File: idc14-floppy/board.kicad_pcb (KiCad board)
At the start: 2 copper layers, 81.3 x 40.3 mm, 10 parts, among them J1 61900411021, J3 2x7, J4 02x17, J5 629105150521, SW1 SW_DPDT_x2

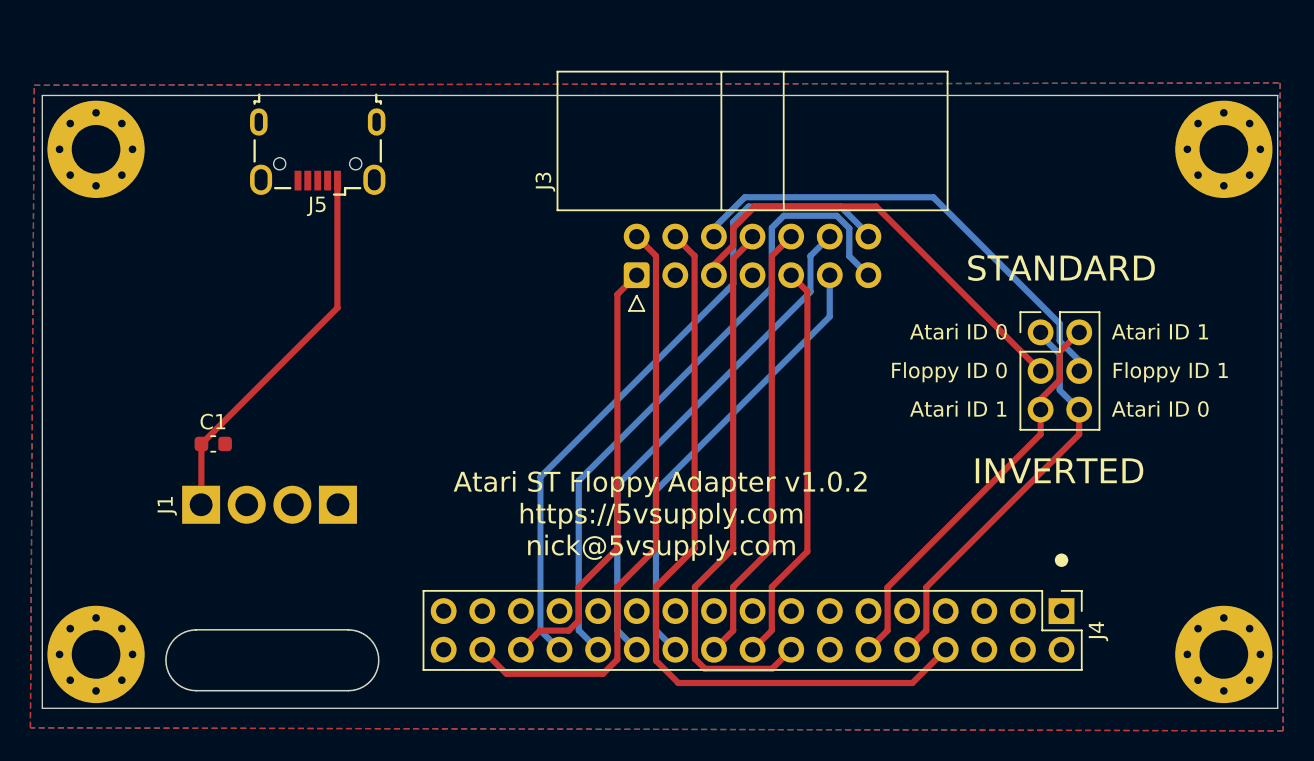
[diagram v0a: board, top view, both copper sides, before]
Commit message: reorganize, start enclosure
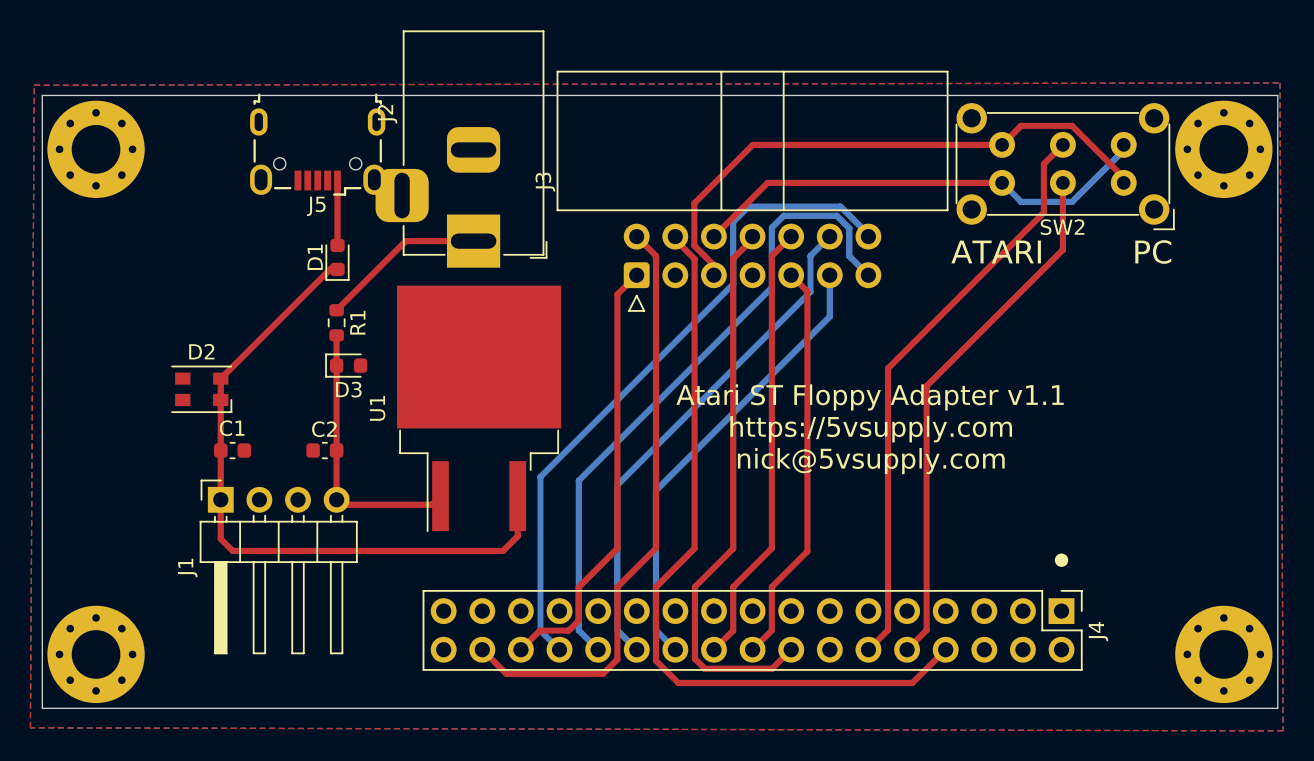
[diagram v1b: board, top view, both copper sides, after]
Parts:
- removed SW1: SW_DPDT_x2, Connector_PinHeader_2.54mm:PinHeader_2x03_P2.54mm_Vertical
- added C2: 2.2uF, Capacitor_SMD:C_0603_1608Metric, F.Cu at (126.5, 108.2)
- added D1: 12v, Diode_SMD:D_0603_1608Metric, F.Cu at (127.3, 95.5)
- added D2: CLM2C-GCA, LED_SMD:LED_Cree-PLCC4_3.2x2.8mm_CCW, F.Cu at (118.4, 104.2)
- added D3: 12v, Diode_SMD:D_0603_1608Metric, F.Cu at (128.0, 102.6)
- added J2: Jack-DC, Connector_BarrelJack:BarrelJack_Horizontal, F.Cu at (136.2, 94.4)
- added R1: 100, Resistor_SMD:R_0603_1608Metric, F.Cu at (127.2, 99.8)
- added SW2: SW_DPDT_x2, Button_Switch_THT:SW_E-Switch_EG2219_DPDT_Angled, F.Cu at (179.0, 90.6)
- added U1: L7805, Package_TO_SOT_SMD:TO-263-2, F.Cu at (136.6, 105.4)
- J1: value 61900411021 -> 171826-4; footprint Connector_PinHeader_2.54mm:PinHeader_1x04_P2.54mm_Vertical -> Connector_PinHeader_2.54mm:PinHeader_1x04_P2.54mm_Horizontal
- moved J1 7.98 mm to (119.6, 119.6)
- moved C1 1.34 mm to (120.4, 108.2)
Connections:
- C1 pad 1: VCC -> +5V
- J1 pad 1: VCC -> +5V
- J1 pad 4: unconnected-(J1-Pad4) -> +12V
- J5 pad 1: VCC -> Net-(J5-Pad1)
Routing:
- net +5V: track 0.00 -> 44.1 mm
- net VCC: track 25.0 -> 0.00 mm
- net +12V: track 0.00 -> 18.6 mm
- net /DRIVE_SEL_B: track 26.6 -> 38.5 mm
- net Net-(J2-Pad1): track 0.00 -> 10.9 mm
- net /FLOPPY_ID0: track 29.3 -> 37.4 mm
- net /DRIVE_SEL_A: track 27.0 -> 35.0 mm
- net Net-(J5-Pad1): track 0.00 -> 4.27 mm
- net /FLOPPY_ID1: track 31.5 -> 30.7 mm
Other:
- outline, holes or cut-outs redrawn
- board text added: "ATARI"
- board text added: "Atari ST Floppy Adapter v1.1 https://5vsupply.com nick@5vsupply.com"
- board text added: "PC"
- board text removed: "Atari ID 0"
- board text removed: "Atari ID 1"
- board text removed: "Atari ST Floppy Adapter v1.0.2 https://5vsupply.com nick@5vsupply.com"
- board text removed: "Floppy ID 0"
- board text removed: "Floppy ID 1"
- board text removed: "INVERTED"
- board text removed: "STANDARD"

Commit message: footprint
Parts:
- removed R1: 100, Resistor_SMD:R_0603_1608Metric
- added R2: 10k, Resistor_SMD:R_0603_1608Metric, F.Cu at (116.0, 106.2)
- added R3: 1.78k, Resistor_SMD:R_0603_1608Metric, F.Cu at (117.5, 103.4)
- added R4: 3.16k, Resistor_SMD:R_0603_1608Metric, F.Cu at (114.4, 103.4)
- D2: value CLM2C-GCA -> LED; footprint LED_SMD:LED_Cree-PLCC4_3.2x2.8mm_CCW -> LED_SMD:LED_0603_1608Metric
- J1: footprint Connector_PinHeader_2.54mm:PinHeader_1x04_P2.54mm_Horizontal -> parts:171826-4
- moved D2 11.6 mm to (113.9, 114.9), turned to 0 degrees
- moved D1 9.57 mm to (119.1, 100.4), turned to 0 degrees
- moved J1 8.24 mm to (122.0, 111.8), turned to 0 degrees
- moved C2 1.43 mm to (125.0, 108.1)
- moved D3 1.43 mm to (126.6, 102.5)
- moved C1 1.31 mm to (119.1, 108.1)
- moved U1 0.57 mm to (136.6, 106.0)
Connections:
- D2 pad 1: +5V -> GND
- D2 pad 2: +5V -> Net-(D2-Pad2)
- J2 pad 1: Net-(J2-Pad1) -> +12V
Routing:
- net +12V: track 18.6 -> 32.1 mm
- net Net-(J2-Pad1): track 10.9 -> 0.00 mm
- net Net-(D1-Pad2): track 4.27 -> 14.3 mm
- net Net-(D2-Pad2): track 0.00 -> 9.59 mm
- net +5V: track 44.1 -> 37.1 mm
- net Net-(R2-Pad2): track 0.00 -> 4.26 mm

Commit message: a
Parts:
- J1: moved to B.Cu
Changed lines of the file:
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@@
       (net 1 "GND") (pinfunction "Pin_1") (pintype "passive"))
-  )
-  (footprint "parts:171826-4" (layer "F.Cu")
-    (at 122.05 111.774)
-    (property "Sheetfile" "board.kicad_sch")
-    (property "Sheetname" "")
-    (fp_text reference "J1" (at 0 2.75) (layer "F.SilkS")
-      (effects (font (size 1 1) (thickness 0.15)))
-    )
-    (fp_text value "171826-4" (at 0 -2.75) (layer "F.Fab")
-      (effects (font (size 1 1) (thickness 0.15)))
-    )
-    (fp_line (start -2.5 -1.75) (end -2.5 1.75) (layer "F.SilkS") (width 0.12))
-    (fp_line (start 5.25 -1.75) (end 5.25 1.75) (layer "F.SilkS") (width 0.12))
-    (fp_line (start -5.25 -1.75) (end 5.25 -1.75) (layer "F.SilkS") (width 0.12))
-    (fp_line (start -5.25 1.75) (end -5.25 -1.75) (layer "F.SilkS") (width 0.12))
-    (fp_line (start 5.25 1.75) (end -5.25 1.75) (layer "F.SilkS") (width 0.12))
-    (fp_line (start -5 -1.5) (end 5 -1.5) (layer "F.CrtYd") (width 0.05))
-    (fp_line (start 5 1.5) (end -5 1.5) (layer "F.CrtYd") (width 0.05))
-    (fp_line (start -5 1.5) (end -5 -1.5) (layer "F.CrtYd") (width 0.05))
-    (fp_line (start 5 -1.5) (end 5 1.5) (layer "F.CrtYd") (width 0.05))
-    (pad "1" thru_hole rect locked (at -3.75 0) (size 1.75 2.5) (drill 0.9) (layers *.Cu *.Mask)
-      (net 2 "+5V") (pinfunction "Pin_1") (pintype "passive"))
-    (pad "2" thru_hole oval (at -1.25 0) (size 1.75 2.5) (drill 0.9) (layers *.Cu *.Mask)
-      (net 1 "GND") (pinfunction "Pin_2") (pintype "passive"))
-    (pad "3" thru_hole oval (at 1.25 0) (size 1.75 2.5) (drill 0.9) (layers *.Cu *.Mask)
-      (net 1 "GND") (pinfunction "Pin_3") (pintype "passive"))
-    (pad "4" thru_hole oval (at 3.75 0) (size 1.75 2.5) (drill 0.9) (layers *.Cu *.Mask)
-      (net 17 "+12V") (pinfunction "Pin_4") (pintype "passive"))
   )
   (footprint "Resistor_SMD:R_0603_1608Metric" (layer "F.Cu")
@@
       (net 1 "GND") (pinfunction "Pin_1") (pintype "passive"))
   )
+  (footprint "parts:171826-4" (layer "B.Cu")
+    (at 122.05 111.774)
+    (property "Sheetfile" "board.kicad_sch")
+    (property "Sheetname" "")
+    (fp_text reference "J1" (at 0 -2.75) (layer "B.SilkS")
+      (effects (font (size 1 1) (thickness 0.15)) (justify mirror))
+    )
+    (fp_text value "171826-4" (at 0 2.75) (layer "B.Fab")
+      (effects (font (size 1 1) (thickness 0.15)) (justify mirror))
+    )
+    (fp_line (start -2.5 1.75) (end -2.5 -1.75) (layer "B.SilkS") (width 0.12))
+    (fp_line (start 5.25 1.75) (end 5.25 -1.75) (layer "B.SilkS") (width 0.12))
+    (fp_line (start -5.25 1.75) (end 5.25 1.75) (layer "B.SilkS") (width 0.12))
+    (fp_line (start -5.25 -1.75) (end -5.25 1.75) (layer "B.SilkS") (width 0.12))
+    (fp_line (start 5.25 -1.75) (end -5.25 -1.75) (layer "B.SilkS") (width 0.12))
+    (fp_line (start -5 1.5) (end 5 1.5) (layer "B.CrtYd") (width 0.05))
+    (fp_line (start 5 -1.5) (end -5 -1.5) (layer "B.CrtYd") (width 0.05))
+    (fp_line (start -5 -1.5) (end -5 1.5) (layer "B.CrtYd") (width 0.05))
+    (fp_line (start 5 1.5) (end 5 -1.5) (layer "B.CrtYd") (width 0.05))
+    (pad "1" thru_hole rect locked (at -3.75 0) (size 1.75 2.5) (drill 0.9) (layers *.Cu *.Mask)
+      (net 2 "+5V") (pinfunction "Pin_1") (pintype "passive"))
+    (pad "2" thru_hole oval (at -1.25 0) (size 1.75 2.5) (drill 0.9) (layers *.Cu *.Mask)
+      (net 1 "GND") (pinfunction "Pin_2") (pintype "passive"))
+    (pad "3" thru_hole oval (at 1.25 0) (size 1.75 2.5) (drill 0.9) (layers *.Cu *.Mask)
+      (net 1 "GND") (pinfunction "Pin_3") (pintype "passive"))
+    (pad "4" thru_hole oval (at 3.75 0) (size 1.75 2.5) (drill 0.9) (layers *.Cu *.Mask)
+      (net 17 "+12V") (pinfunction "Pin_4") (pintype "passive"))
+  )
   (gr_circle (center 174.9094 115.4176) (end 175.275724 115.4176) (layer "F.SilkS") (width 0.15) (fill solid))
